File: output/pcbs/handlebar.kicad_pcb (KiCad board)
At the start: 4 copper layers, 153.6 x 106.8 mm, 111 parts

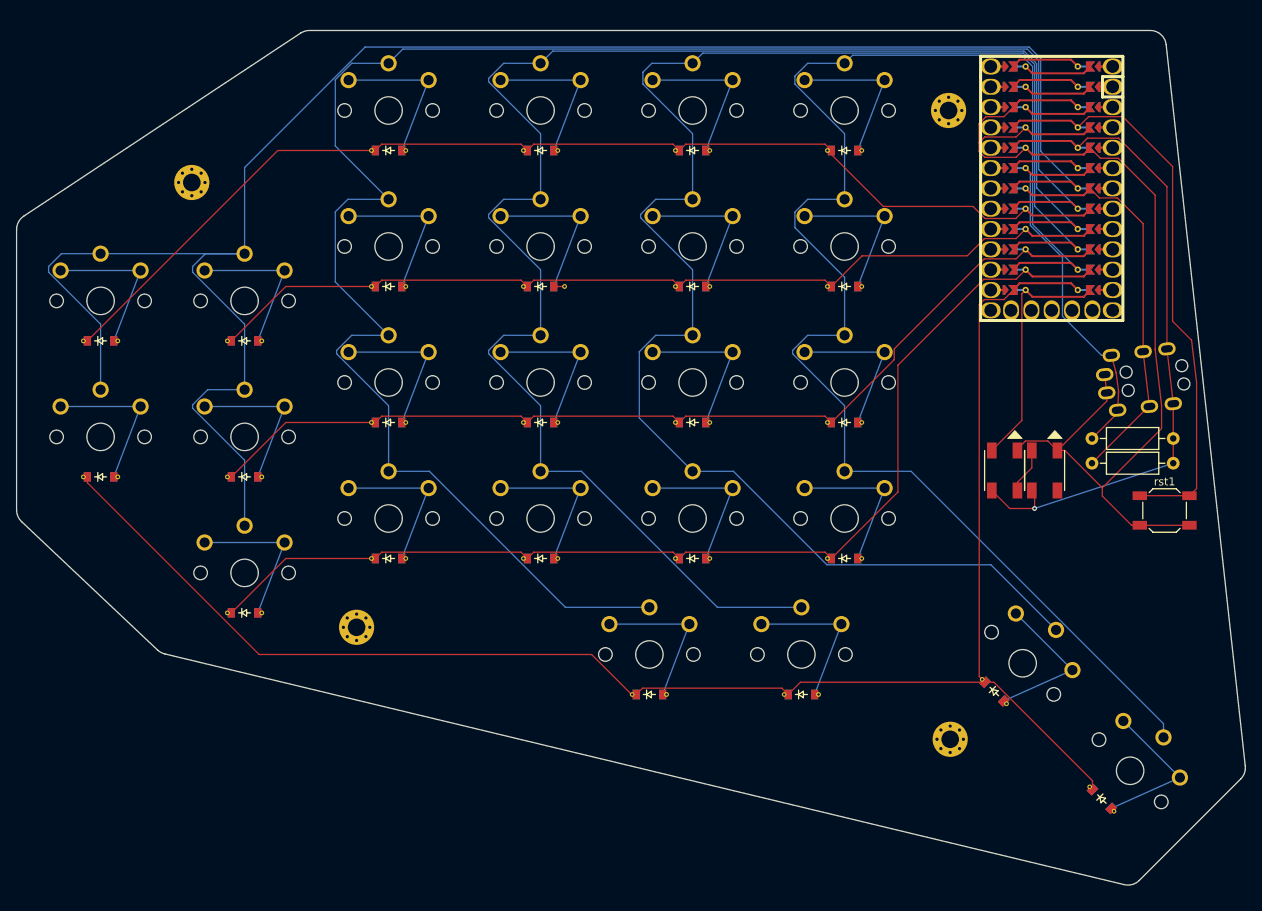
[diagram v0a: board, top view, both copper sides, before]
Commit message: Updated gitignore
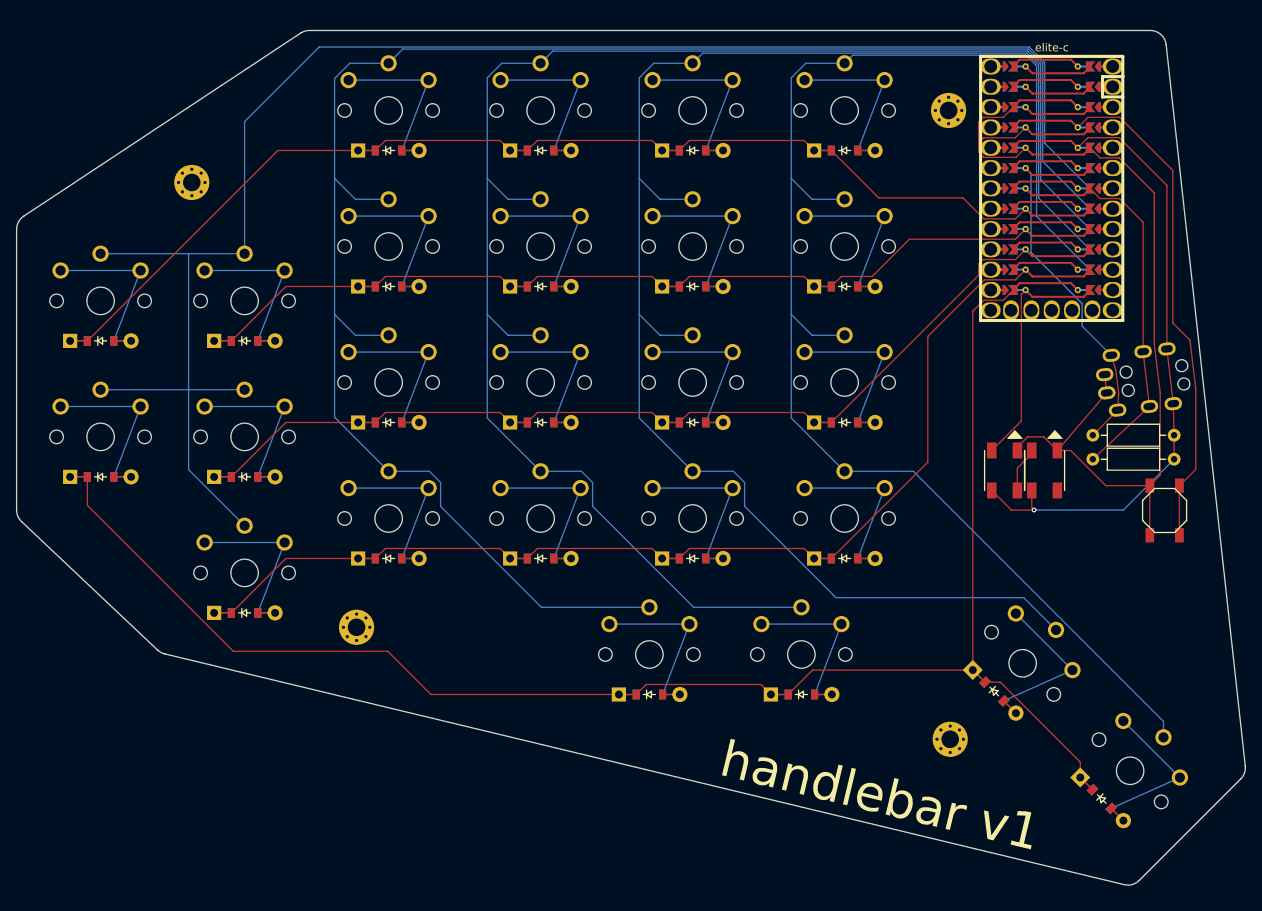
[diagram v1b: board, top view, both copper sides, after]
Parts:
- removed the REF** at (102.2, 88.0)
- removed the REF** at (116.8, 54.0)
- removed the REF** at (61.9, 77.8)
- removed the REF** at (130.4, 122.0)
- removed the REF** at (122.0, 71.0)
- removed the REF** at (187.9, 90.0)
- removed the REF** at (140.2, 88.0)
- removed the REF** at (79.8, 94.8)
- removed the REF** at (135.8, 71.0)
- removed the REF** at (116.8, 71.0)
- removed the REF** at (97.8, 54.0)
- removed the REF** at (154.8, 88.0)
- removed the REF** at (140.2, 54.0)
- removed the REF** at (187.6, 133.6)
- removed the REF** at (102.2, 105.0)
- removed the REF** at (174.2, 120.1)
- removed the REF** at (66.2, 94.8)
- removed the REF** at (140.2, 71.0)
- removed the REF** at (177.2, 123.2)
- removed the REF** at (190.7, 136.6)
- removed the REF** at (134.8, 122.0)
- removed the REF** at (153.8, 122.0)
- removed the REF** at (154.8, 105.0)
- removed the REF** at (159.2, 88.0)
- removed the REF** at (159.2, 54.0)
- removed the REF** at (84.2, 94.8)
- removed the REF** at (116.8, 105.0)
- removed the REF** at (159.2, 71.0)
- removed the REF** at (79.8, 111.8)
- removed the REF** at (159.2, 105.0)
- removed the REF** at (149.4, 122.0)
- removed the REF** at (135.8, 88.0)
- removed the REF** at (102.2, 71.0)
- removed the REF** at (135.8, 54.0)
- removed the REF** at (116.8, 88.0)
- removed the REF** at (97.8, 71.0)
- removed the REF** at (135.8, 105.0)
- removed the REF** at (84.2, 77.8)
- removed the REF** at (140.2, 105.0)
- removed the REF** at (84.2, 111.8)
- removed the REF** at (102.2, 54.0)
- removed the REF** at (61.9, 94.8)
- removed the REF** at (121.2, 105.0)
- removed the REF** at (121.2, 54.0)
- removed the REF** at (97.8, 105.0)
- removed the REF** at (154.8, 54.0)
- removed the REF** at (97.8, 88.0)
- removed the REF** at (79.8, 77.8)
- removed the REF** at (154.8, 71.0)
- removed the REF** at (121.2, 88.0)
- removed the REF** at (187.9, 93.1)
- removed the REF** at (66.2, 77.8)
- removed _52, _53, _54, _55: , MountingHole:MountingHole_2.2mm_M2_Pad_Via
- added REF**: R_Axial_DIN0207_L6.3mm_D2.5mm_P10.16mm_Horizontal, Resistor_THT:R_Axial_DIN0207_L6.3mm_D2.5mm_P10.16mm_Horizontal, F.Cu at (188.0, 89.6)
- added REF**: R_Axial_DIN0207_L6.3mm_D2.5mm_P10.16mm_Horizontal, Resistor_THT:R_Axial_DIN0207_L6.3mm_D2.5mm_P10.16mm_Horizontal, F.Cu at (188.0, 92.6)
- added _2: , MountingHole_2.2mm_M2_Pad_Via, F.Cu at (75.4, 58.0)
- added _3: , MountingHole_2.2mm_M2_Pad_Via, F.Cu at (96.0, 113.6)
- added _4: , MountingHole_2.2mm_M2_Pad_Via, F.Cu at (170.0, 49.0)
- added _5: , MountingHole_2.2mm_M2_Pad_Via, F.Cu at (170.2, 127.6)
- rst1: footprint Button_Switch_SMD:SW_SPST_SKQG_WithoutStem -> E73:SW_TACT_ALPS_SKQGABE010
- turned rst1 to -90 degrees
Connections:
- net _51_1 renamed _1_1
- net _51_10 renamed _1_10
- net _51_11 renamed _1_11
- net _51_14 renamed _1_14
- net _51_15 renamed _1_15
- net _51_16 renamed _1_16
- net _51_17 renamed _1_17
- net _51_18 renamed _1_18
- net _51_19 renamed _1_19
- net _51_2 renamed _1_2
- net _51_20 renamed _1_20
- net _51_21 renamed _1_21
- net _51_22 renamed _1_22
- net _51_23 renamed _1_23
- net _51_24 renamed _1_24
- net _51_3 renamed _1_3
- net _51_4 renamed _1_4
- net _51_5 renamed _1_5
- net _51_6 renamed _1_6
- net _51_7 renamed _1_7
- net _51_8 renamed _1_8
- net _51_9 renamed _1_9
- ? pad 0: _51_0 -> VBUS
- ? pad 25: _51_25 -> VBUS
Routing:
- net VBUS: track 0.00 -> 28.6 mm
- net n_pinky: track 239.1 -> 222.4 mm
- net n_thumb: track 207.7 -> 222.9 mm
- net _51_0: track 14.3 -> 0.00 mm
- net _51_25: track 14.3 -> 0.00 mm
- net n_home: track 124.1 -> 138.3 mm
- net n_top: track 117.3 -> 131.4 mm
- net n_bottom: track 138.6 -> 152.6 mm
- net n_nums: track 143.9 -> 157.6 mm
- net center_thumb: track 19.4 -> 23.7 mm
- net inner_thumb: track 19.4 -> 23.7 mm
- net ring_top: track 19.4 -> 23.7 mm
- net ring_nums: track 19.4 -> 23.7 mm
- net ring_home: track 19.4 -> 23.7 mm
- net ring_bottom: track 19.4 -> 23.7 mm
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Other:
- board text added: "handlebar v1"

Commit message: Changed the big name. Better parts list.
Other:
- board text added: "handlebar"
- board text removed: "handlebar v1"

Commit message: v1 complete and sent to maker
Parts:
- removed the REF** at (188.0, 89.6)
- removed the REF** at (188.0, 92.6)
- added REF**: R_Axial_DIN0207_L6.3mm_D2.5mm_P10.16mm_Horizontal, Resistor_THT:R_Axial_DIN0207_L6.3mm_D2.5mm_P10.16mm_Horizontal, F.Cu at (188.2, 93.0)
- added REF**: R_Axial_DIN0207_L6.3mm_D2.5mm_P10.16mm_Horizontal, Resistor_THT:R_Axial_DIN0207_L6.3mm_D2.5mm_P10.16mm_Horizontal, F.Cu at (188.2, 89.7)
- I1, I2: footprint Personal:WS2812B -> Library:WS2812B
- rst1: footprint E73:SW_TACT_ALPS_SKQGABE010 -> Library:SW_TACT_ALPS_SKQGABE010
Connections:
- net _1_1 renamed D3
- net _1_2 renamed D2
- ? pad 10: _1_10 -> n_bottom
- ? pad 11: _1_11 -> n_indic
- ? pad 3: _1_3 -> n_gnd
- ? pad 4: _1_4 -> n_gnd
- ? pad 5: _1_5 -> n_sda
- ? pad 6: _1_6 -> n_scl
- ? pad 7: _1_7 -> n_nums
- ? pad 8: _1_8 -> n_top
- ? pad 9: _1_9 -> n_home
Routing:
- net _1_24: track 14.3 -> 4.00 mm
- net _1_20: track 14.3 -> 4.00 mm
- net F4: track 0.00 -> 10.3 mm
- net B0: track 0.00 -> 10.3 mm
- net VBUS: track 28.6 -> 20.6 mm
- net (no net): track 0.00 -> 8.00 mm
- net _1_2: track 0.00 -> 4.00 mm
- net _1_1: track 0.00 -> 4.00 mm
- net D3: track 14.3 -> 10.3 mm
- net D2: track 14.3 -> 10.3 mm
- net n_pinky: track 222.4 -> 220.1 mm
- net n_inner: track 193.2 -> 191.0 mm
- net n_index: track 210.6 -> 208.6 mm
- net n_ring: track 230.6 -> 228.9 mm
- net n_middle: track 213.5 -> 212.2 mm
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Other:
- board text added: "v1"
